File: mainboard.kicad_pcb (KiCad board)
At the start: 2 copper layers, 157.6 x 135.8 mm, 57 parts, among them J1 DRV8833-1, J13 Conn_PCA9685, J14 Conn_01x02, J15 Conn_01x02, J16 Conn_01x02, J18 Screw_Terminal_01x06, J19 Screw_Terminal_01x06, J2 DRV8833-0, J20 Screw_Terminal_01x06, J21 Screw_Terminal_01x06, J22 Screw_Terminal_01x06, J23 Screw_Terminal_01x06, J24 Screw_Terminal_01x04, J25 Screw_Terminal_01x02, J27 Rotary Encoder Conn, J28 Conn_01x02, J3 Conn_01x02, J4 Screw_Terminal_01x06, J5 Screw_Terminal_01x06, J6 VIM4_HEADER, J7 Screw_Terminal_01x06, J8 Screw_Terminal_01x06, Q3 2N7000, Q4 2N7000, U1 MCP23017_SP

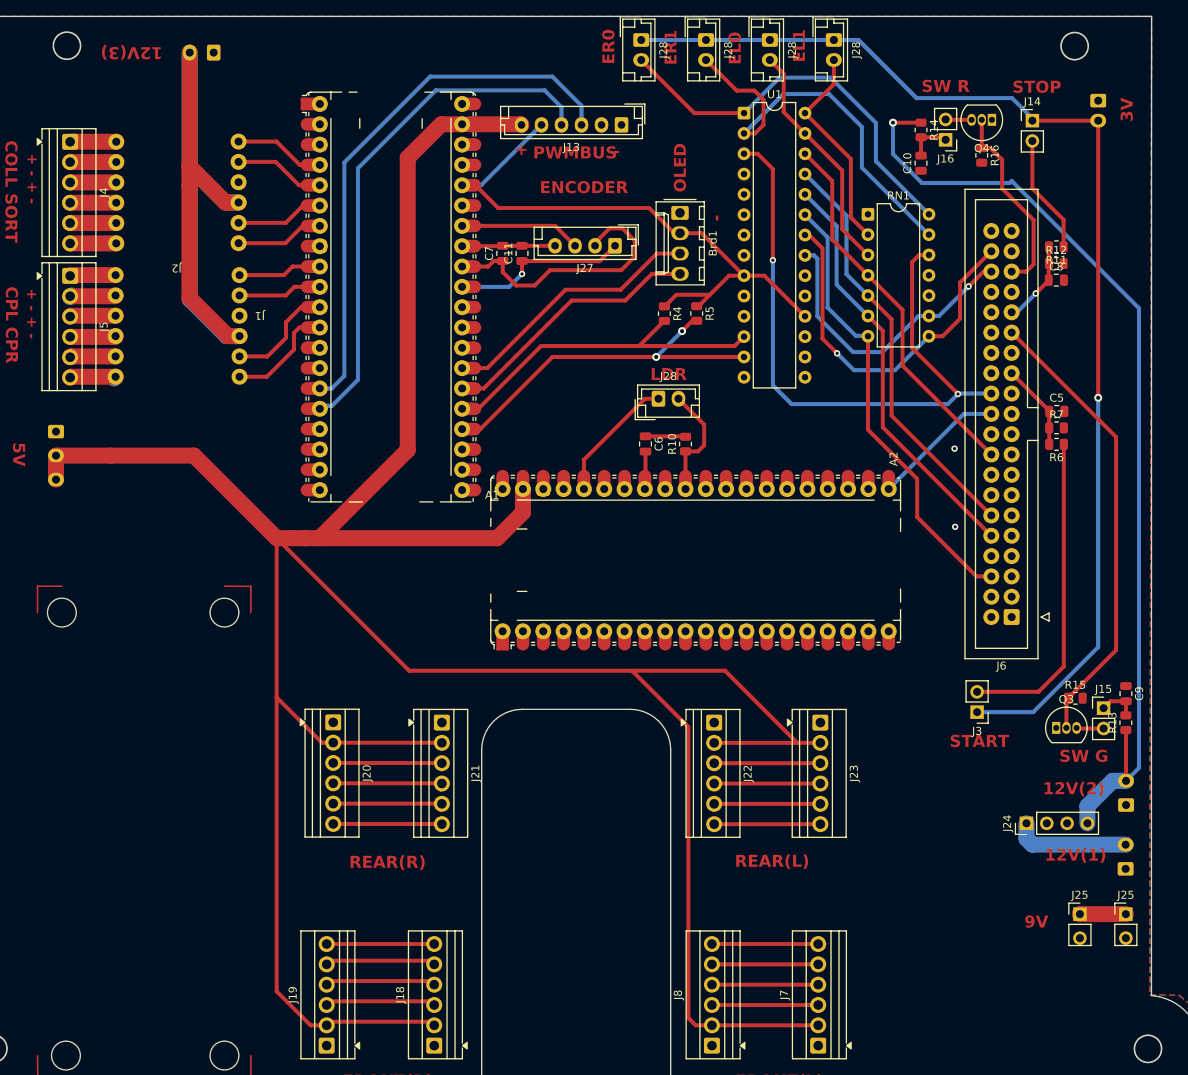
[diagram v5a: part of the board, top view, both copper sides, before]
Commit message: Buckboard Beta 1
Ready for Ochoa review
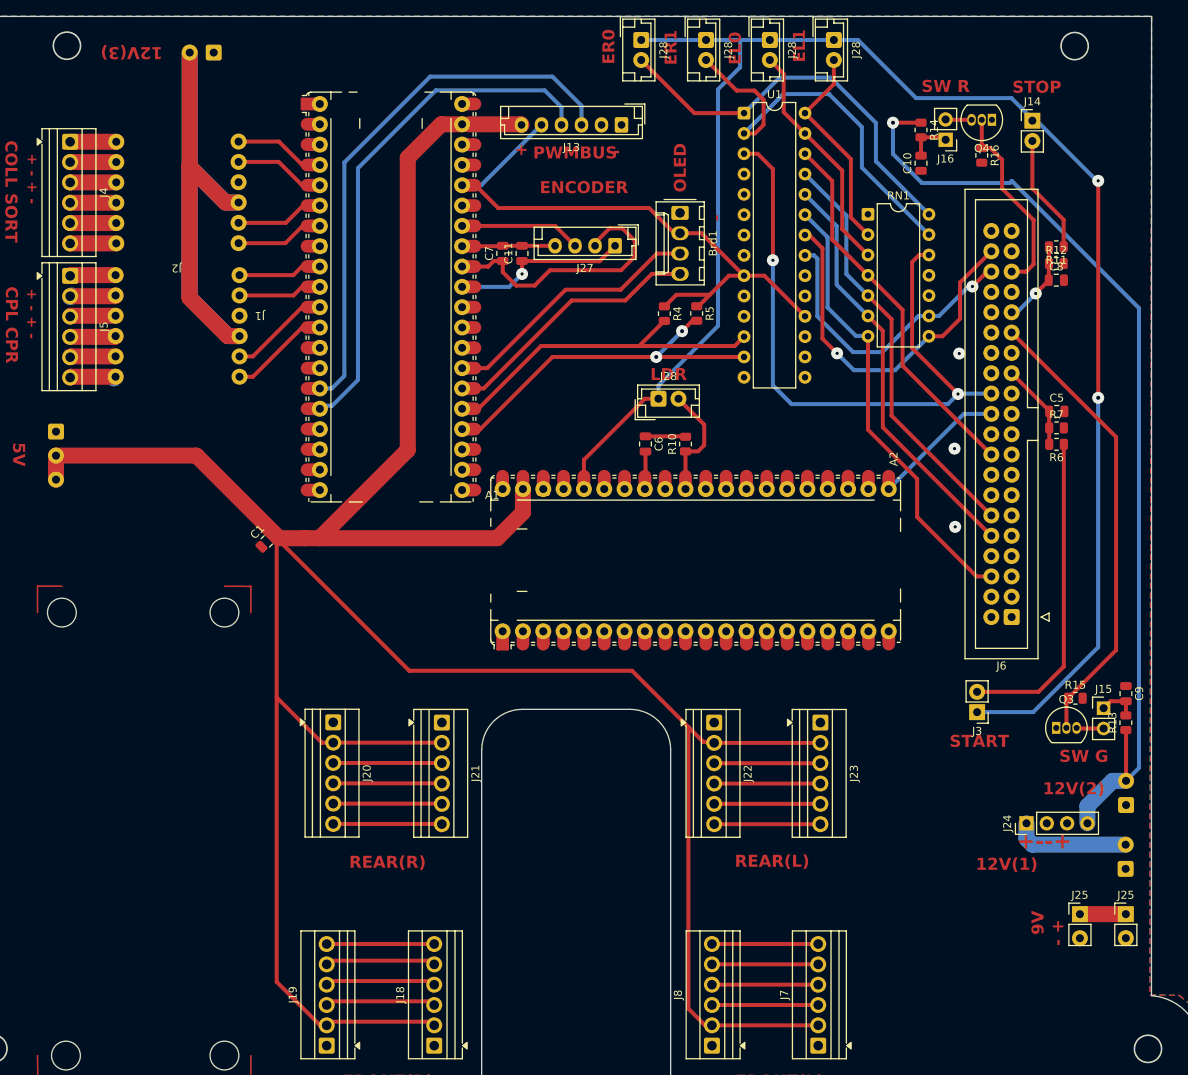
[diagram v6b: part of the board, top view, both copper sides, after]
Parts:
- removed the ? at (400.8, 46.0)
- added C1: 1uF, Capacitor_SMD:C_0805_2012Metric, F.Cu at (296.9, 98.6)
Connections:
- J14 pad 1: 3V_BUCK -> PICO2_3V3
- J28 pad 1: 3V_BUCK -> PICO2_3V3 (x4)
- J3 pad 1: 3V_BUCK -> PICO2_3V3
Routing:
- net PICO2_3V3: track 15.3 -> 205.9 mm, vias 0 -> 2
- net 3V_BUCK: track 145.7 -> 0.00 mm, vias 1 -> 0
- net 5V_BUCK: track 390.5 -> 368.8 mm
- net Net-(A1-GPIO9): track 13.0 -> 11.8 mm
- net Net-(A1-GPIO8): track 12.9 -> 11.8 mm
- net GND: vias 2 -> 3
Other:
- board text added: "+--+"
- board text added: "- +"
- board text removed: "3V"

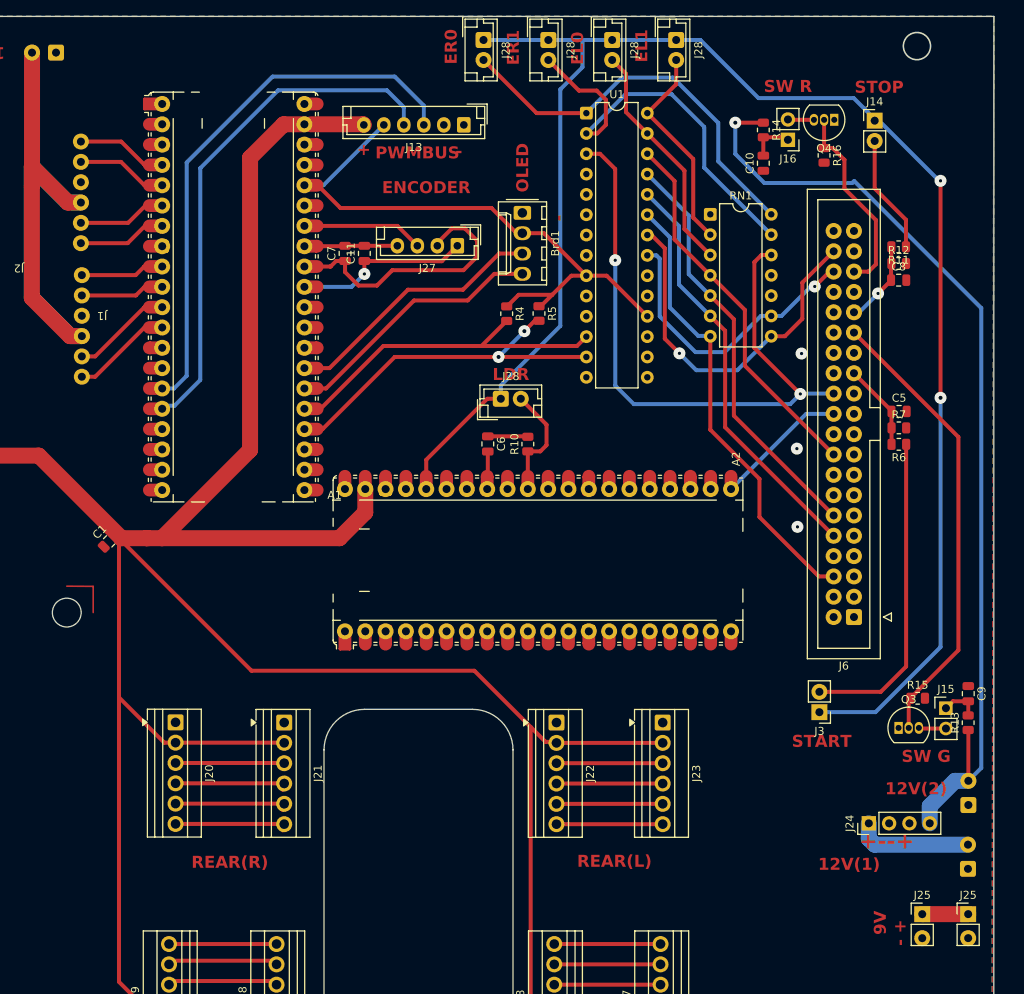
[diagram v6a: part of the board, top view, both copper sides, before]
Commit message: Displayboard added
V1 of displayboard, this includes the SSD1309 and EC11 Rotary encoder with 1x04 JST connectors at 2.5mm pitch
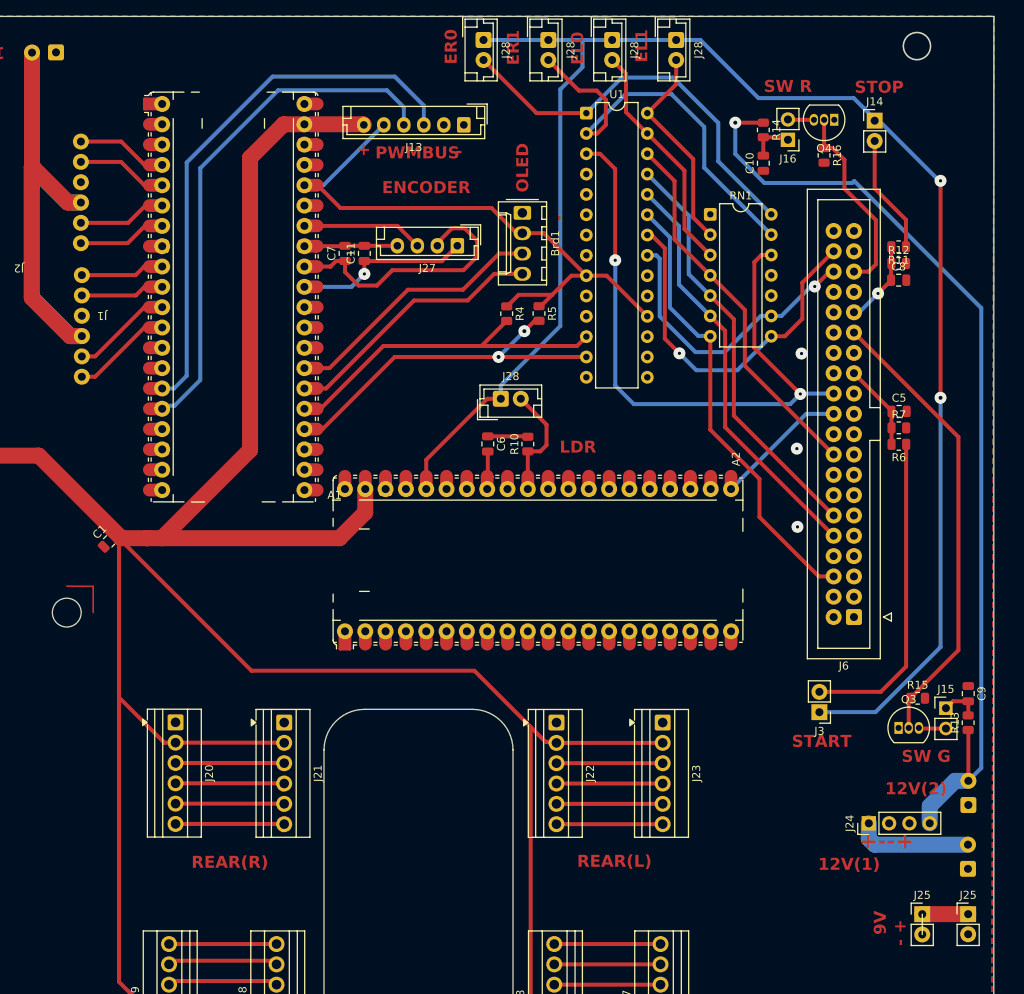
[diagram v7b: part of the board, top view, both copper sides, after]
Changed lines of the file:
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@@
 		(embedded_fonts no)
 		(model "${KICAD9_3DMODEL_DIR}/Connector_Molex.3dshapes/Molex_KK-254_AE-6410-04A_1x04_P2.54mm_Vertical.step"
+			(hide yes)
+			(offset
+				(xyz 0 0 0)
+			)
+			(scale
+				(xyz 1 1 1)
+			)
+			(rotate
+				(xyz 0 0 0)
+			)
+		)
+		(model "${KICAD9_3DMODEL_DIR}/Connector_JST.3dshapes/JST_EH_B4B-EH-A_1x04_P2.50mm_Vertical.wrl"
 			(offset
 				(xyz 0 0 0)
@@
 		)
 		(fp_line
+			(start 0 0)
+			(end 0 2.54)
+			(stroke
+				(width 0.1)
+				(type default)
+			)
+			(layer "F.SilkS")
+		)
+		(fp_line
 			(start 1.38 1.27)
 			(end 1.38 3.92)
@@
 		)
 		(pad "2" thru_hole circle
-			(at 0 3)
-			(size 2 1.7)
+			(at 0 2.54)
+			(size 2 2)
 			(drill 1)
 			(layers "*.Cu" "*.Mask")
@@
 		)
 		(pad "1" thru_hole roundrect
-			(at -3 0 180)
+			(at -2.9972 0.0254 180)
 			(size 2 2)
 			(drill 1)
@@
 		)
 		(pad "2" thru_hole circle
-			(at 0 3)
-			(size 2 1.7)
+			(at 0 2.5146)
+			(size 2 2)
 			(drill 1)
 			(layers "*.Cu" "*.Mask")
@@
 	)
 	(gr_text "LDR"
-		(at 344.795195 78.584805 0)
+		(at 353.177195 87.665205 0)
 		(layer "F.Cu")
 		(effects

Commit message: V1.2
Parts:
- added ?: , clipboard:9c2f8d19-4101-4f98-a26c-8554f3c2bdce, F.Cu at (289.9, 91.8)
- added ?: , , F.Cu at (334.2, 82.3)
- added ?: , , F.Cu at (377.5, 134.6)
- added ?: , , F.Cu at (309.2, 37.5)
- added ?: , , F.Cu at (326.7, 70.5)
- added ?: , , F.Cu at (383.1, 96.8)
- added ?: , , F.Cu at (375.7, 61.9)
- added C1: 1uF, Capacitor_SMD:C_0805_2012Metric, B.Cu at (293.1, 89.1)
- added REF**: TestPoint_THTPad_D2.0mm_Drill1.0mm, TestPoint:TestPoint_THTPad_D2.0mm_Drill1.0mm, F.Cu at (351.0, 51.3)
- added REF**: TestPoint_THTPad_D2.0mm_Drill1.0mm, TestPoint:TestPoint_THTPad_D2.0mm_Drill1.0mm, F.Cu at (276.6, 99.6)
- C1, C10, C11, C5, C6, C7, C8, C9, R10, R11, R12, R13, R14, R15, R16, R4, R5, R6, R7: moved to B.Cu
- moved ? 19.4 mm to (289.8, 86.4)
- moved Q3 9.93 mm to (386.7, 126.4)
- moved J28 8.20 mm to (343.6, 35.9)
- moved J28 8.10 mm to (351.8, 35.9)
- moved R15 7.00 mm to (393.0, 123.2), turned to 90 degrees
- moved R12 6.96 mm to (395.6, 70.8)
- moved J24 6.10 mm to (392.6, 139.9), turned to 180 degrees
- moved J25 5.48 mm to (398.5, 150.7)
- moved J25 5.48 mm to (404.3, 150.7)
- moved R11 4.25 mm to (395.6, 66.0)
- moved ? 4.15 mm to (404.4, 140.6)
- moved R4 2.74 mm to (343.8, 70.1)
- moved C8 2.43 mm to (395.6, 68.4)
- moved ? 2.20 mm to (287.2, 39.7)
- moved C1 1.93 mm to (295.5, 99.9)
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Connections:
- J13 pad 6: 5V_BUCK -> 5V_BUCK2
- J14 pad 1: PICO2_3V3 -> PICO1_3V3
- J28 pad 1: PICO2_3V3 -> PICO1_3V3 (x4)
- J3 pad 1: PICO2_3V3 -> PICO1_3V3
- J6 pad 22: unconnected-(J6-Pin_22-Pad22) -> COLL(en/dis)
- J6 pad 30: unconnected-(J6-Pin_30-Pad30) -> SORT(en/dis)
- J6 pad 31: PIC_STATE -> TOTEM-EXTEND
- J6 pad 32: TOTEM-EXTEND -> unconnected-(J6-Pin_32-Pad32)
- J6 pad 33: BOOM(ext/ret) -> unconnected-(J6-Pin_33-Pad33)
- J6 pad 36: unconnected-(J6-Pin_36-Pad36) -> PIC_STATE
- J6 pad 38: COLL(en/dis) -> unconnected-(J6-Pin_38-Pad38)
- J6 pad 39: SORT(en/dis) -> unconnected-(J6-Pin_39-Pad39)
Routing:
- net PICO2_3V3: track 205.9 -> 15.3 mm, vias 2 -> 0
- net PICO1_3V3: track 75.7 -> 246.0 mm, vias 0 -> 2
- net 12V_BUCK3: track 93.8 -> 44.7 mm
- net COLL(en/dis): track 36.8 -> 65.8 mm
- net PIC_STATE: track 16.7 -> 42.4 mm
- net 5V_BUCK: track 368.8 -> 348.2 mm
- net SORT(en/dis): track 45.9 -> 58.8 mm, vias 1 -> 2
- net Net-(J15-Pin_2): track 3.41 -> 12.8 mm
- net TOTEM-EXTEND: track 81.6 -> 90.7 mm, vias 2 -> 4
- net 12V_BUCK2: track 120.8 -> 127.4 mm, vias 1 -> 0
- net CP-R-ENDSTOP0: track 50.4 -> 44.3 mm
- net CP-L-ENDSTOP1: track 26.7 -> 32.5 mm, vias 0 -> 1
- net GREEN: track 57.4 -> 62.5 mm, vias 0 -> 2
- net CP-L-ENDSTOP0: track 29.5 -> 33.7 mm, vias 0 -> 1
- net Net-(J14-Pin_2): track 15.1 -> 19.1 mm, vias 0 -> 2
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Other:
- outline, holes or cut-outs redrawn
- board text added: "+-+-"
- board text added: "12V1"
- board text added: "12V2"
- board text added: "12V3"
- board text added: "5V1"
- board text added: "USB"
- board text removed: "+--+"
- board text removed: "12V(1)"
- board text removed: "12V(2)"
- board text removed: "12V(3)"
- board text removed: "5V"
